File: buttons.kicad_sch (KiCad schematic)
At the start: 11 parts, among them SW1 power, SW2 up, SW3 down, SW4 left, SW5 rigth

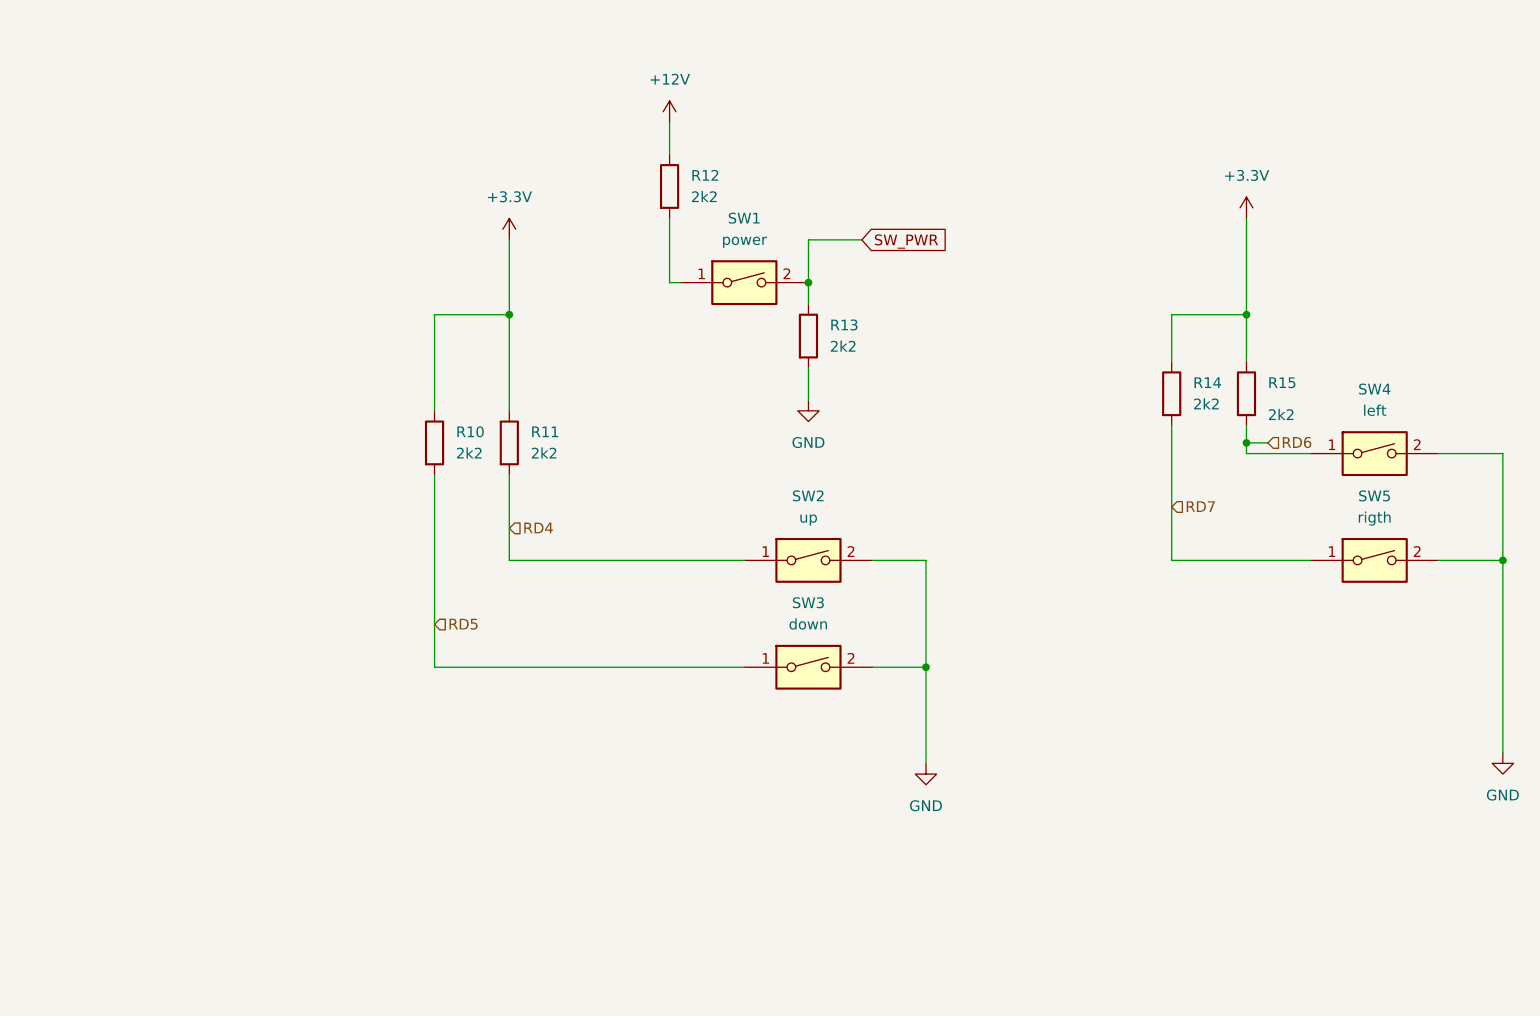
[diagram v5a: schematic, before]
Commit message: feat: 2-layer stackup, bus net class and schematic cleanup
PCB / project
- Reduce board from 4 layers to 2 (F.Cu / B.Cu) for cheaper fabrication
- Add "bus" net class and reorder net class priorities (bus 0, usb_differential 1, ...)

Schematics
- usb_conector_Ft232: add D+ / D-- labels on the USB mini-B data pair
- ft232: add 10K pull-ups, 100nf decoupling and test points on +3.3VA
- tp_ft232: remove solder jumpers JP1/JP2 (TX_Rpi / RX_Rpi now direct)
- Usb_pic32: add C38 100nf decoupling on +5V
- oled: expand connector J25 from 7 to 8 pins
- mcu / idc / power / zigbee / buttons / cnc_pic32: annotation and net cleanup

docs
- Add USB-Mini-B pinout reference images
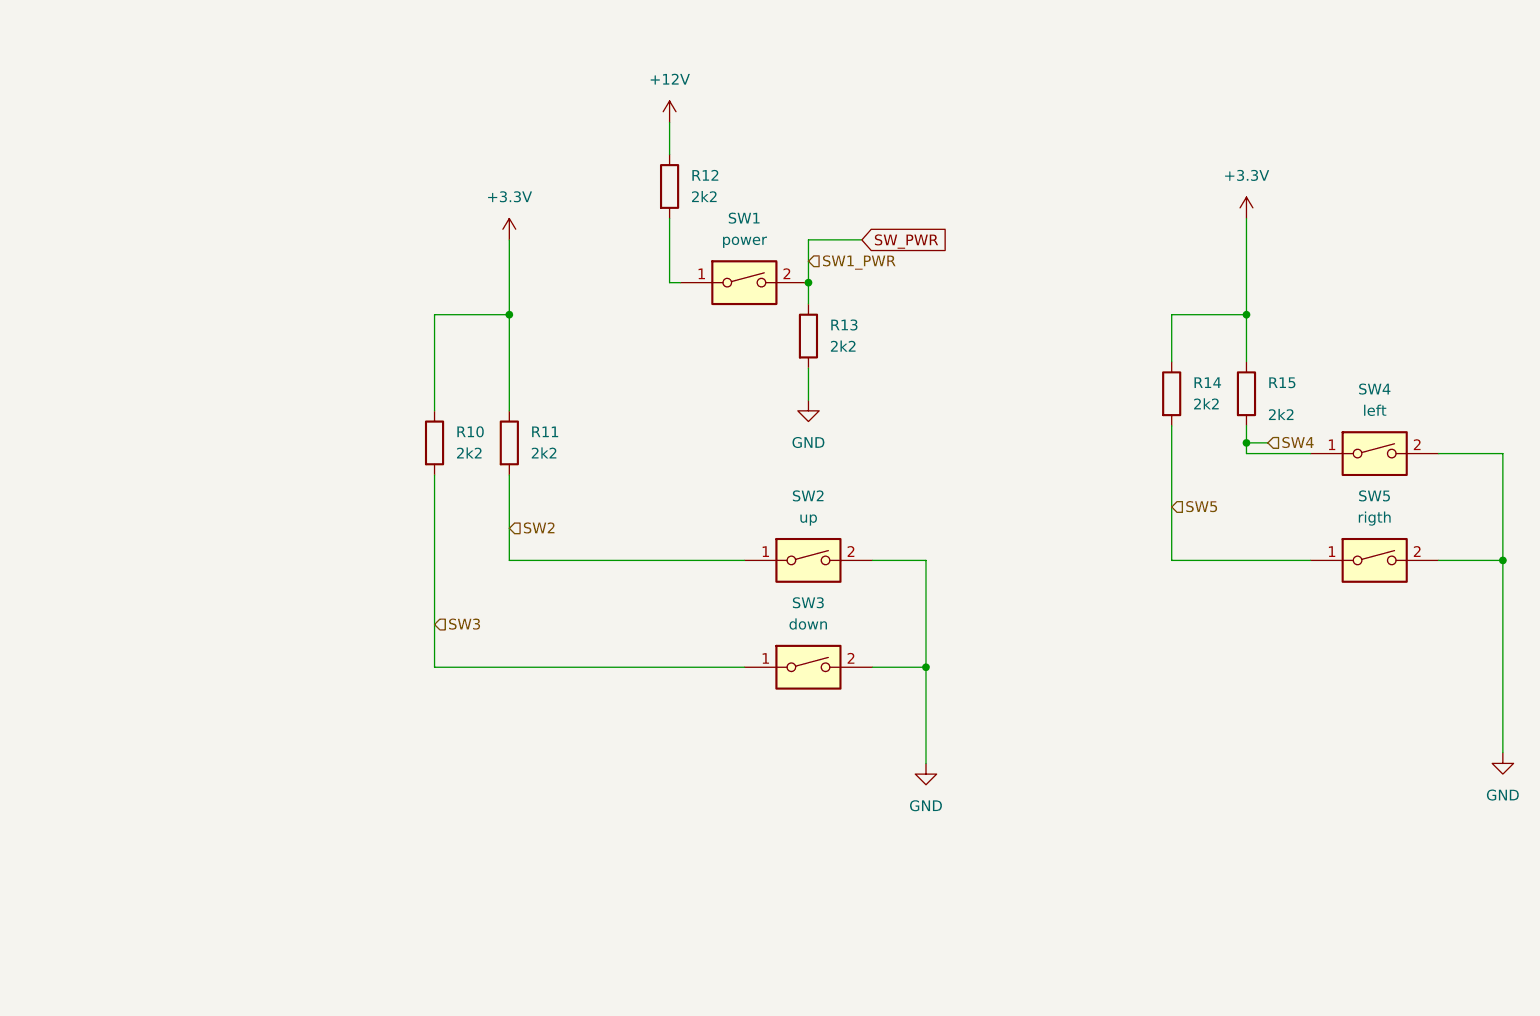
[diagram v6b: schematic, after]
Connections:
- net RD4 renamed SW2
- net RD5 renamed SW3
- net RD6 renamed SW4
- net RD7 renamed SW5
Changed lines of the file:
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@@
 		)
 	)
-	(hierarchical_label "RD4"
+	(hierarchical_label "SW2"
 		(shape input)
 		(at 109.22 106.68 0)
@@
 		)
 	)
-	(hierarchical_label "RD5"
+	(hierarchical_label "SW3"
 		(shape input)
 		(at 100.33 118.11 0)
@@
 		)
 	)
-	(hierarchical_label "RD7"
+	(hierarchical_label "SW1_PWR"
+		(shape input)
+		(at 144.78 74.93 0)
+		(effects
+			(font
+				(size 1.27 1.27)
+			)
+			(justify left)
+		)
+	)
+	(hierarchical_label "SW5"
 		(shape input)
 		(at 187.96 104.14 0)
@@
 		)
 	)
-	(hierarchical_label "RD6"
+	(hierarchical_label "SW4"
 		(shape input)
 		(at 199.39 96.52 0)
@@
 		(instances
 			(project "cnc_pic32"
-				(path "/13dbfc1f-be47-44ca-9042-3d6a9a657d7d/64cf98d4-7353-423c-baad-4e05534717be/fed6e348-19f5-499e-8dbd-e696ef87e744"
+				(path "/13dbfc1f-be47-44ca-9042-3d6a9a657d7d/c23451d0-70ea-4fb8-9f51-b04cd7803801"
 					(reference "SW5")
 					(unit 1)
@@
 		(instances
 			(project "cnc_pic32"
-				(path "/13dbfc1f-be47-44ca-9042-3d6a9a657d7d/64cf98d4-7353-423c-baad-4e05534717be/fed6e348-19f5-499e-8dbd-e696ef87e744"
+				(path "/13dbfc1f-be47-44ca-9042-3d6a9a657d7d/c23451d0-70ea-4fb8-9f51-b04cd7803801"
 					(reference "SW1")
 					(unit 1)
@@
 		(instances
 			(project "cnc_pic32"
-				(path "/13dbfc1f-be47-44ca-9042-3d6a9a657d7d/64cf98d4-7353-423c-baad-4e05534717be/fed6e348-19f5-499e-8dbd-e696ef87e744"
+				(path "/13dbfc1f-be47-44ca-9042-3d6a9a657d7d/c23451d0-70ea-4fb8-9f51-b04cd7803801"
 					(reference "R14")
 					(unit 1)
@@
 		(instances
 			(project "cnc_pic32"
-				(path "/13dbfc1f-be47-44ca-9042-3d6a9a657d7d/64cf98d4-7353-423c-baad-4e05534717be/fed6e348-19f5-499e-8dbd-e696ef87e744"
+				(path "/13dbfc1f-be47-44ca-9042-3d6a9a657d7d/c23451d0-70ea-4fb8-9f51-b04cd7803801"
 					(reference "R15")
 					(unit 1)
@@
 		(instances
 			(project "cnc_pic32"
-				(path "/13dbfc1f-be47-44ca-9042-3d6a9a657d7d/64cf98d4-7353-423c-baad-4e05534717be/fed6e348-19f5-499e-8dbd-e696ef87e744"
+				(path "/13dbfc1f-be47-44ca-9042-3d6a9a657d7d/c23451d0-70ea-4fb8-9f51-b04cd7803801"
 					(reference "#PWR019")
 					(unit 1)
@@
 		(instances
 			(project "cnc_pic32"
-				(path "/13dbfc1f-be47-44ca-9042-3d6a9a657d7d/64cf98d4-7353-423c-baad-4e05534717be/fed6e348-19f5-499e-8dbd-e696ef87e744"
+				(path "/13dbfc1f-be47-44ca-9042-3d6a9a657d7d/c23451d0-70ea-4fb8-9f51-b04cd7803801"
 					(reference "R13")
 					(unit 1)
@@
 		(instances
 			(project "cnc_pic32"
-				(path "/13dbfc1f-be47-44ca-9042-3d6a9a657d7d/64cf98d4-7353-423c-baad-4e05534717be/fed6e348-19f5-499e-8dbd-e696ef87e744"
+				(path "/13dbfc1f-be47-44ca-9042-3d6a9a657d7d/c23451d0-70ea-4fb8-9f51-b04cd7803801"
 					(reference "R10")
 					(unit 1)
@@
 		(instances
 			(project "cnc_pic32"
-				(path "/13dbfc1f-be47-44ca-9042-3d6a9a657d7d/64cf98d4-7353-423c-baad-4e05534717be/fed6e348-19f5-499e-8dbd-e696ef87e744"
+				(path "/13dbfc1f-be47-44ca-9042-3d6a9a657d7d/c23451d0-70ea-4fb8-9f51-b04cd7803801"
 					(reference "#PWR018")
 					(unit 1)
@@
 		(instances
 			(project "cnc_pic32"
-				(path "/13dbfc1f-be47-44ca-9042-3d6a9a657d7d/64cf98d4-7353-423c-baad-4e05534717be/fed6e348-19f5-499e-8dbd-e696ef87e744"
+				(path "/13dbfc1f-be47-44ca-9042-3d6a9a657d7d/c23451d0-70ea-4fb8-9f51-b04cd7803801"
 					(reference "SW3")
 					(unit 1)
@@
 		(instances
 			(project "cnc_pic32"
-				(path "/13dbfc1f-be47-44ca-9042-3d6a9a657d7d/64cf98d4-7353-423c-baad-4e05534717be/fed6e348-19f5-499e-8dbd-e696ef87e744"
+				(path "/13dbfc1f-be47-44ca-9042-3d6a9a657d7d/c23451d0-70ea-4fb8-9f51-b04cd7803801"
 					(reference "#PWR016")
 					(unit 1)
@@
 		(instances
 			(project "cnc_pic32"
-				(path "/13dbfc1f-be47-44ca-9042-3d6a9a657d7d/64cf98d4-7353-423c-baad-4e05534717be/fed6e348-19f5-499e-8dbd-e696ef87e744"
+				(path "/13dbfc1f-be47-44ca-9042-3d6a9a657d7d/c23451d0-70ea-4fb8-9f51-b04cd7803801"
 					(reference "SW4")
 					(unit 1)
@@
 		(instances
 			(project "cnc_pic32"
-				(path "/13dbfc1f-be47-44ca-9042-3d6a9a657d7d/64cf98d4-7353-423c-baad-4e05534717be/fed6e348-19f5-499e-8dbd-e696ef87e744"
+				(path "/13dbfc1f-be47-44ca-9042-3d6a9a657d7d/c23451d0-70ea-4fb8-9f51-b04cd7803801"
 					(reference "#PWR014")
 					(unit 1)
@@
 		(instances
 			(project "cnc_pic32"
-				(path "/13dbfc1f-be47-44ca-9042-3d6a9a657d7d/64cf98d4-7353-423c-baad-4e05534717be/fed6e348-19f5-499e-8dbd-e696ef87e744"
+				(path "/13dbfc1f-be47-44ca-9042-3d6a9a657d7d/c23451d0-70ea-4fb8-9f51-b04cd7803801"
 					(reference "#PWR017")
 					(unit 1)
@@
 		(instances
 			(project "cnc_pic32"
-				(path "/13dbfc1f-be47-44ca-9042-3d6a9a657d7d/64cf98d4-7353-423c-baad-4e05534717be/fed6e348-19f5-499e-8dbd-e696ef87e744"
+				(path "/13dbfc1f-be47-44ca-9042-3d6a9a657d7d/c23451d0-70ea-4fb8-9f51-b04cd7803801"
 					(reference "SW2")
 					(unit 1)
@@
 		(instances
 			(project "cnc_pic32"
-				(path "/13dbfc1f-be47-44ca-9042-3d6a9a657d7d/64cf98d4-7353-423c-baad-4e05534717be/fed6e348-19f5-499e-8dbd-e696ef87e744"
+				(path "/13dbfc1f-be47-44ca-9042-3d6a9a657d7d/c23451d0-70ea-4fb8-9f51-b04cd7803801"
 					(reference "R11")
 					(unit 1)
@@
 		(instances
 			(project "cnc_pic32"
-				(path "/13dbfc1f-be47-44ca-9042-3d6a9a657d7d/64cf98d4-7353-423c-baad-4e05534717be/fed6e348-19f5-499e-8dbd-e696ef87e744"
+				(path "/13dbfc1f-be47-44ca-9042-3d6a9a657d7d/c23451d0-70ea-4fb8-9f51-b04cd7803801"
 					(reference "#PWR015")
 					(unit 1)
@@
 		(instances
 			(project "cnc_pic32"
-				(path "/13dbfc1f-be47-44ca-9042-3d6a9a657d7d/64cf98d4-7353-423c-baad-4e05534717be/fed6e348-19f5-499e-8dbd-e696ef87e744"
+				(path "/13dbfc1f-be47-44ca-9042-3d6a9a657d7d/c23451d0-70ea-4fb8-9f51-b04cd7803801"
 					(reference "R12")
 					(unit 1)

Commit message: updated
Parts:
- added D6, D7, D8: LED, Diode_SMD:D_0805_2012Metric, symbol Device:LED
- added R3, R50, R51: 1k, Resistor_SMD:R_0805_2012Metric, symbol Device:R
- SW1: value power -> K2-1107ST-A4SW-06; footprint Button_Switch_SMD:SW_SPST_CK_RS282G05A3 -> Button_Switch_SMD:SW_Tactile_SPST_NO_Straight_CK_PTS636Sx25SMTRLFS
- SW2: value up -> K2-1107ST-A4SW-06; footprint Button_Switch_SMD:SW_SPST_CK_RS282G05A3 -> Button_Switch_SMD:SW_Tactile_SPST_NO_Straight_CK_PTS636Sx25SMTRLFS
- SW3: value down -> K2-1107ST-A4SW-06; footprint Button_Switch_SMD:SW_SPST_CK_RS282G05A3 -> Button_Switch_SMD:SW_Tactile_SPST_NO_Straight_CK_PTS636Sx25SMTRLFS
- SW4: value left -> K2-1107ST-A4SW-06; footprint Button_Switch_SMD:SW_SPST_CK_RS282G05A3 -> Button_Switch_SMD:SW_Tactile_SPST_NO_Straight_CK_PTS636Sx25SMTRLFS
- SW5: value rigth -> K2-1107ST-A4SW-06; footprint Button_Switch_SMD:SW_SPST_CK_RS282G05A3 -> Button_Switch_SMD:SW_Tactile_SPST_NO_Straight_CK_PTS636Sx25SMTRLFS
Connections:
- net GND: now also R3.2, R50.2, R51.2
- net +12V renamed VCC
- new net: D8.1 (K), R51.1
- new net: D7.1 (K), R50.1
- new net: D6.1 (K), R3.1
- new net led1: D6.2 (A)
- new net led2: D7.2 (A)
- new net led3: D8.2 (A)
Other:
- note added: "posible push C49234124 otro recomendado C118141 4 patas comprado en mouser C127478 switch value SKQGAKE010 4 patas C127478 foot: Button_Switch_SMD:SW_SPST_TL3342"
